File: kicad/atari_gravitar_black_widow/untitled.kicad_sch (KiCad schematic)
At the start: 53 parts

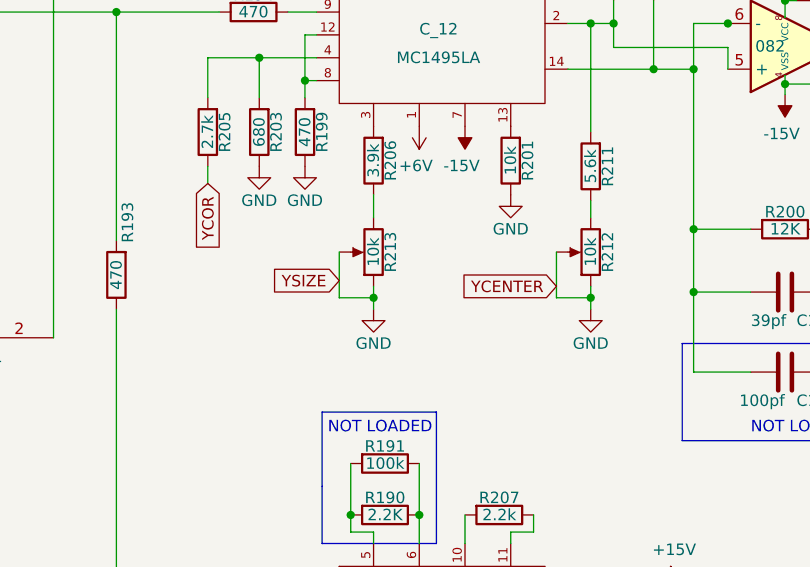
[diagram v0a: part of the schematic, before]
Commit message: Worked on removing the warnings
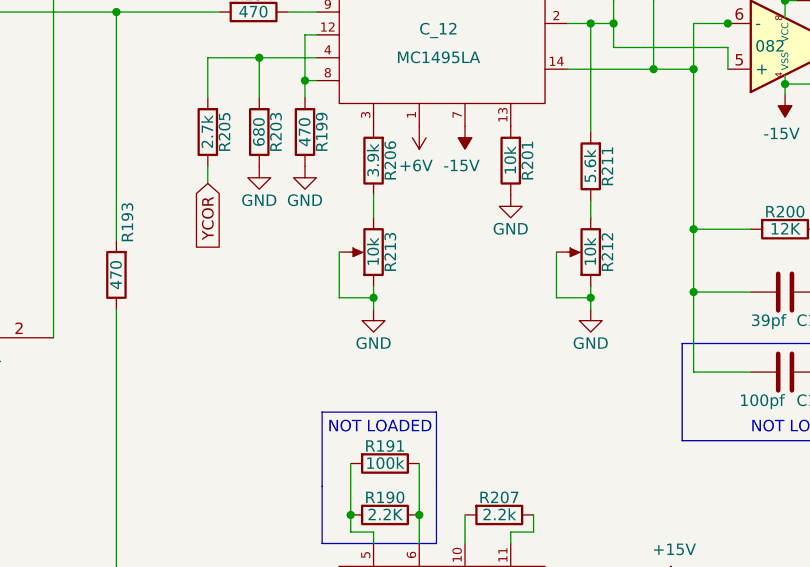
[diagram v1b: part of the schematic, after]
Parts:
- E_10: footprint Star_Wars_Vector_PCB:DIP16 -> (none)
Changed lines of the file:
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@@
-    )
-  )
-  (global_label "YCENTER" (shape input) (at 474.726 196.596 180) (fields_autoplaced)
-    (effects (font (size 1.27 1.27)) (justify right))
-    (property "Intersheet References" "${INTERSHEET_REFS}" (id 0) (at 464.177 196.5166 0)
-      (effects (font (size 1.27 1.27)) (justify right) hide)
     )
   )
@@
     (effects (font (size 1.27 1.27)) (justify right))
     (property "Intersheet References" "${INTERSHEET_REFS}" (id 0) (at 18.7397 178.1016 0)
-      (effects (font (size 1.27 1.27)) (justify right) hide)
-    )
-  )
-  (global_label "YSIZE" (shape input) (at 450.596 195.961 180) (fields_autoplaced)
-    (effects (font (size 1.27 1.27)) (justify right))
-    (property "Intersheet References" "${INTERSHEET_REFS}" (id 0) (at 443.0104 195.8816 0)
       (effects (font (size 1.27 1.27)) (justify right) hide)
     )
@@
     (property "Reference" "E_10" (id 0) (at 390.906 184.531 0))
     (property "Value" "LF13201" (id 1) (at 386.461 190.881 0))
-    (property "Footprint" "Star_Wars_Vector_PCB:DIP16" (id 2) (at 390.906 187.706 0)
+    (property "Footprint" "" (id 2) (at 390.906 187.706 0)
       (effects (font (size 1.524 1.524)) hide)
     )
@@
     (pin "3")
   )
-  (symbol (lib_name "LF13201_1") (lib_id "Star_Wars_Vector_PCB:LF13201") (at 532.638 206.121 0) (unit 2)
+  (symbol (lib_id "Star_Wars_Vector_PCB:LF13201") (at 532.638 206.121 0) (unit 2)
     (in_bom yes) (on_board yes) (fields_autoplaced)
     (property "Reference" "E_10" (id 0) (at 532.638 220.8435 0))
@@
     (property "Reference" "E_10" (id 0) (at 390.906 159.131 0))
     (property "Value" "LF13201" (id 1) (at 383.921 154.686 0))
-    (property "Footprint" "Star_Wars_Vector_PCB:DIP16" (id 2) (at 390.906 155.956 0)
+    (property "Footprint" "" (id 2) (at 390.906 155.956 0)
       (effects (font (size 1.524 1.524)) hide)
     )
@@
     (property "Reference" "E_10" (id 0) (at 336.296 159.131 0))
     (property "Value" "LF13201" (id 1) (at 343.281 154.686 0))
-    (property "Footprint" "Star_Wars_Vector_PCB:DIP16" (id 2) (at 336.296 155.956 0)
+    (property "Footprint" "" (id 2) (at 336.296 155.956 0)
       (effects (font (size 1.524 1.524)) hide)
     )

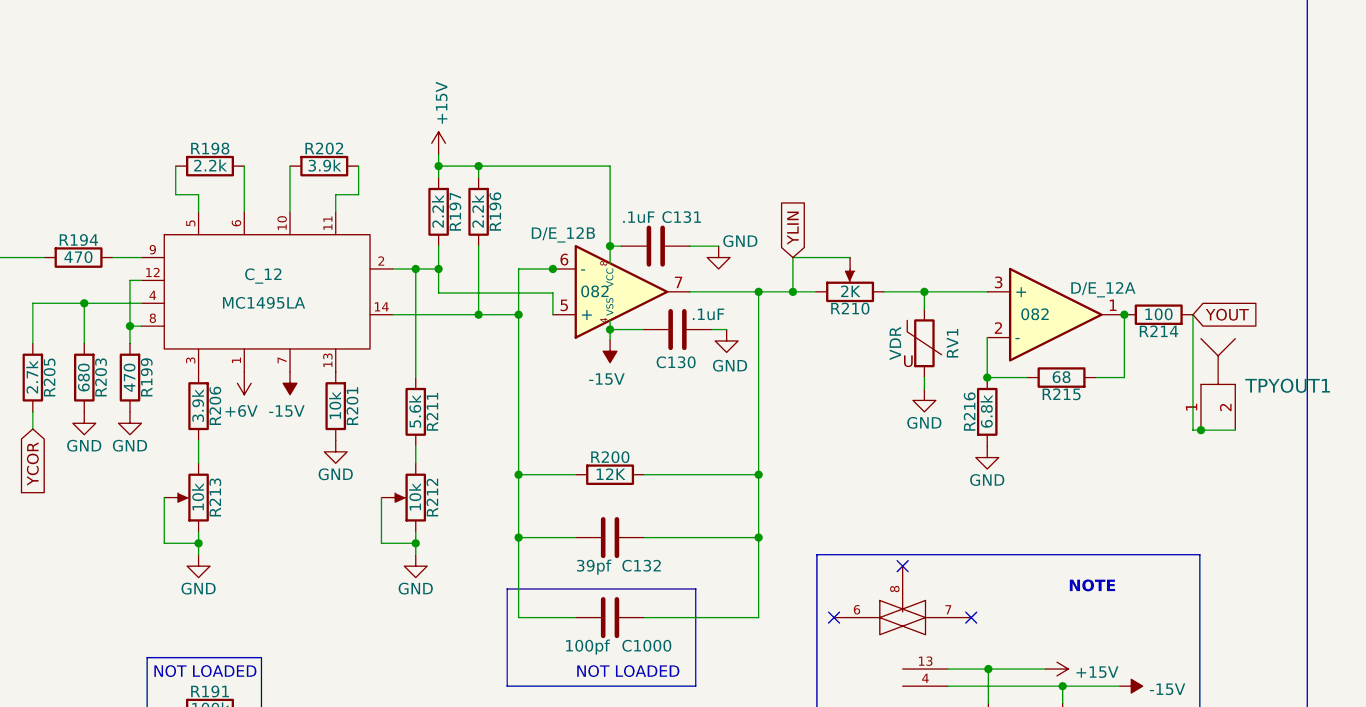
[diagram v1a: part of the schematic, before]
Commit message: Removed more warnings - 25 warnings remain
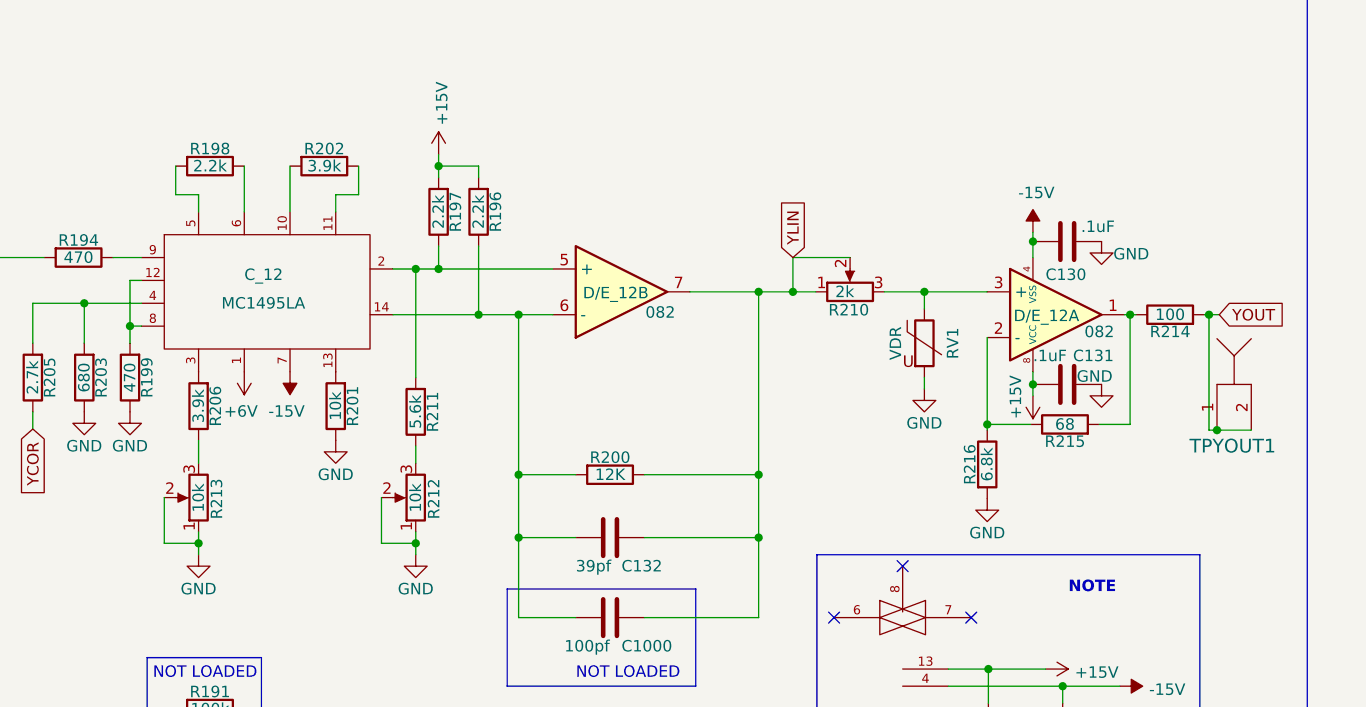
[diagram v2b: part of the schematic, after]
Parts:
- removed D/E_12: 082, symbol Star_Wars_Vector_PCB:082
- removed R210: 2K, Star_Wars_Vector_PCB:PotBlk, symbol Star_Wars_Vector_PCB-rescue:POT
- removed R212, R213: 10k, Star_Wars_Vector_PCB:PotBlk, symbol Star_Wars_Vector_PCB-rescue:POT
- added D/E_12: 082, symbol atari_grav_bw:082
- added R210: 2k, symbol atari_grav_bw:POT
- added R212, R213: 10k, symbol atari_grav_bw:POT
- A/B_12, C_12: footprint Star_Wars_Vector_PCB:DIP14 -> (none)
- C1000, C132, C65: footprint quantum_arcade_pcb:CapSmall -> (none)
- C130, C131, C134, C135, C136, C64, C66, C81, C82, C83, C84, R190, R191, R193, R194, R196, R197, R198, R199, R200, R201, R202, R203, R204, R205, R206, R207, R208, R209, R211, R214, R215, R216, R83, R84, R96, R97, RV1: footprint quantum_arcade_pcb:GenComp -> (none)
- C72: footprint quantum_arcade_pcb:CapInt -> (none)
- D_10: footprint Star_Wars_Vector_PCB:DIP8 -> (none)
- F_9: footprint Star_Wars_Vector_PCB:DIP20 -> (none)
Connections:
- net +15V: now also D/E_12.8 (VCC)
- net -15V: now also D/E_12.4 (VSS)
- net GND: now also R212.1, R212.2, R213.1, R213.2
- net YLIN: now also D/E_12.7, R210.1, R210.2
- net at C_12.2, R197.1, R211.2: now also D/E_12.5 (+)
- net at C1000.2, C132.2, C_12.14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: now also D/E_12.6 (-)
- net at R206.1: now also R213.3
- net at RV1.1: now also D/E_12.3 (+), R210.3
- net at R211.1: now also R212.3
- net at R214.1, R215.2: now also D/E_12.1
- net at R215.1, R216.1: now also D/E_12.2 (-)
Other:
- moved on the sheet: C130, C131, R214, R215, R216, TPYOUT1

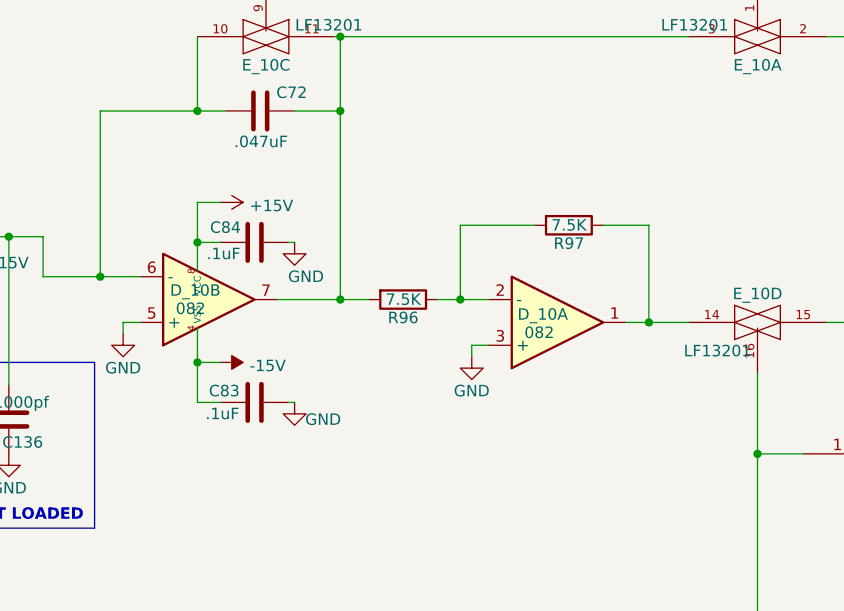
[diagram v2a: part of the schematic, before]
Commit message: Fixed all warnings and errors
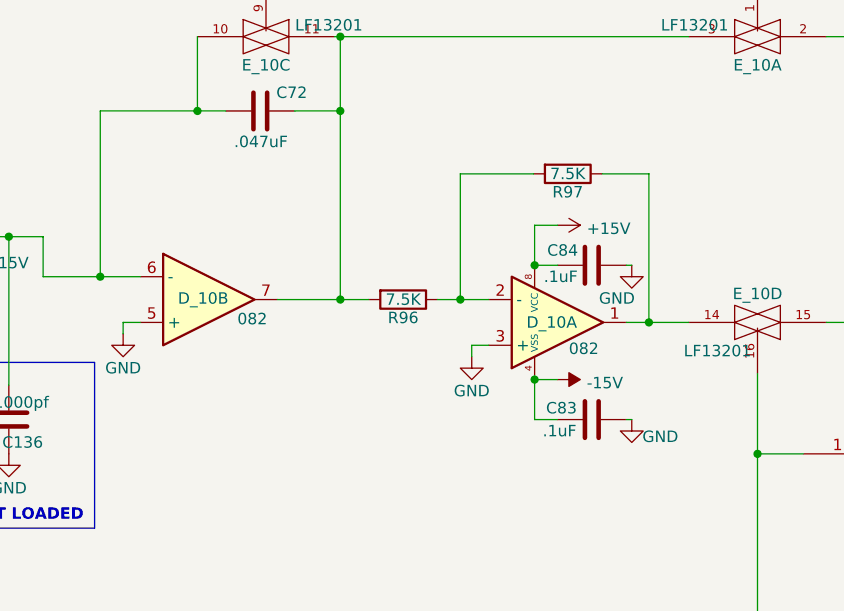
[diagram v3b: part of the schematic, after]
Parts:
- removed D_10: 082, symbol Star_Wars_Vector_PCB:082
- added D_10: 082, symbol atari_grav_bw:082
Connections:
- net +15V: now also D_10.8 (VCC)
- net -15V: now also D_10.4 (VSS)
- net GND: now also D_10.3 (+), D_10.5 (+)
- net YBIP: now also D_10.6 (-)
- net at C72.1, E_10.11, E_10.3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: now also D_10.7
- net at E_10.14, R97.1: now also D_10.1
- net at R96.1, R97.2: now also D_10.2 (-)
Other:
- moved on the sheet: C83, C84, R97

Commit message: more ttl placements
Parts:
- C_12: footprint (none) -> Star_Wars_Vector_PCB:DIP14
- D_10: footprint (none) -> Star_Wars_Vector_PCB:DIP8
- E_10: footprint (none) -> Star_Wars_Vector_PCB:DIP16
- F_9: footprint (none) -> Star_Wars_Vector_PCB:DIP20
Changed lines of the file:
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@@
     (property "Reference" "E_10" (id 0) (at 390.906 184.531 0))
     (property "Value" "LF13201" (id 1) (at 386.461 190.881 0))
-    (property "Footprint" "" (id 2) (at 390.906 187.706 0)
+    (property "Footprint" "Star_Wars_Vector_PCB:DIP16" (id 2) (at 390.906 187.706 0)
       (effects (font (size 1.524 1.524)) hide)
     )
@@
     (property "Reference" "D_10" (id 0) (at 329.311 185.039 0))
     (property "Value" "082" (id 1) (at 334.772 187.325 0))
-    (property "Footprint" "" (id 2) (at 329.946 185.166 0)
+    (property "Footprint" "Star_Wars_Vector_PCB:DIP8" (id 2) (at 329.946 185.166 0)
       (effects (font (size 1.27 1.27)) hide)
     )
@@
       (effects (font (size 1.27 1.27)) (justify left))
     )
-    (property "Footprint" "" (id 2) (at 462.026 169.926 0)
+    (property "Footprint" "Star_Wars_Vector_PCB:DIP14" (id 2) (at 462.026 169.926 0)
       (effects (font (size 1.27 1.27)) hide)
     )
@@
     (property "Reference" "E_10" (id 0) (at 532.638 220.8435 0))
     (property "Value" "LF13201" (id 1) (at 532.638 223.6186 0))
-    (property "Footprint" "" (id 2) (at 532.638 206.121 0)
+    (property "Footprint" "Star_Wars_Vector_PCB:DIP16" (id 2) (at 532.638 206.121 0)
       (effects (font (size 1.524 1.524)) hide)
     )
@@
     (property "Reference" "E_10" (id 0) (at 390.906 159.131 0))
     (property "Value" "LF13201" (id 1) (at 383.921 154.686 0))
-    (property "Footprint" "" (id 2) (at 390.906 155.956 0)
+    (property "Footprint" "Star_Wars_Vector_PCB:DIP16" (id 2) (at 390.906 155.956 0)
       (effects (font (size 1.524 1.524)) hide)
     )
@@
     (property "Reference" "E_10" (id 0) (at 336.296 159.131 0))
     (property "Value" "LF13201" (id 1) (at 343.281 154.686 0))
-    (property "Footprint" "" (id 2) (at 336.296 155.956 0)
+    (property "Footprint" "Star_Wars_Vector_PCB:DIP16" (id 2) (at 336.296 155.956 0)
       (effects (font (size 1.524 1.524)) hide)
     )
@@
     (property "Reference" "D_10" (id 0) (at 368.046 187.706 0))
     (property "Value" "082" (id 1) (at 371.602 190.627 0))
-    (property "Footprint" "" (id 2) (at 368.681 187.706 0)
+    (property "Footprint" "Star_Wars_Vector_PCB:DIP8" (id 2) (at 368.681 187.706 0)
       (effects (font (size 1.27 1.27)) hide)
     )
@@
     (property "Reference" "F_9" (id 0) (at 265.176 184.531 0))
     (property "Value" "AM6012" (id 1) (at 265.176 191.516 90))
-    (property "Footprint" "" (id 2) (at 265.176 183.261 0)
-      (effects (font (size 1.27 1.27)) hide)
-    )
+    (property "Footprint" "Star_Wars_Vector_PCB:DIP20" (id 2) (at 265.176 183.261 0)
+      (effects (font (size 1.27 1.27)) hide)
+    )

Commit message: more chip layouts
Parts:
- D/E_12: footprint (none) -> Star_Wars_Vector_PCB:DIP8
- K_9: footprint (none) -> Star_Wars_Vector_PCB:DIP14
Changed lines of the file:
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@@
     (property "Reference" "K_9" (id 0) (at 410.21 199.898 0))
     (property "Value" "LS04" (id 1) (at 410.972 204.724 0))
-    (property "Footprint" "" (id 2) (at 407.416 202.311 0)
+    (property "Footprint" "Star_Wars_Vector_PCB:DIP14" (id 2) (at 407.416 202.311 0)
       (effects (font (size 1.27 1.27)) hide)
     )
@@
     (property "Reference" "D/E_12" (id 0) (at 500.761 170.053 0))
     (property "Value" "082" (id 1) (at 505.714 172.212 0))
-    (property "Footprint" "" (id 2) (at 501.396 169.926 0)
+    (property "Footprint" "Star_Wars_Vector_PCB:DIP8" (id 2) (at 501.396 169.926 0)
       (effects (font (size 1.27 1.27)) hide)
     )
@@
       (effects (font (size 1.27 1.27)) (justify left))
     )
-    (property "Footprint" "" (id 2) (at 549.656 172.466 0)
-      (effects (font (size 1.27 1.27)) hide)
-    )
+    (property "Footprint" "Star_Wars_Vector_PCB:DIP8" (id 2) (at 549.656 172.466 0)
+      (effects (font (size 1.27 1.27)) hide)
+    )

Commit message: placements
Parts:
- A/B_12: footprint (none) -> Star_Wars_Vector_PCB:DIP14
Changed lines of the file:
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@@
       (effects (font (size 1.27 1.27)) (justify left))
     )
-    (property "Footprint" "" (id 2) (at 462.026 234.061 0)
+    (property "Footprint" "Star_Wars_Vector_PCB:DIP14" (id 2) (at 462.026 234.061 0)
       (effects (font (size 1.27 1.27)) hide)
     )

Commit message: TEST POINTS PLACED
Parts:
- TPYOUT1: footprint (none) -> quantum_arcade_pcb:TP
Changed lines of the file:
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@@
       (effects (font (size 1.524 1.524)) hide)
     )
-    (property "Footprint" "" (id 2) (at 567.563 181.483 0)
+    (property "Footprint" "quantum_arcade_pcb:TP" (id 2) (at 567.563 181.483 0)
       (effects (font (size 1.524 1.524)) hide)
     )

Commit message: C16-30
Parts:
- C64: footprint (none) -> Star_Wars_Vector_PCB:GenericComp
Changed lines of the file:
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@@
       (effects (font (size 1.27 1.27)) (justify left))
     )
-    (property "Footprint" "" (id 2) (at 257.556 165.8112 0)
+    (property "Footprint" "Star_Wars_Vector_PCB:GenericComp" (id 2) (at 257.556 165.8112 0)
       (effects (font (size 1.27 1.27)) hide)
     )
